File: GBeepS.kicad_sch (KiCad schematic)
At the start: 64 parts, among them J1 Ant, J2 BAT_TAB_POS, J3 BAT_TAB_NEGATIVE, Q1 PMZ130UNEYL, Q2 PMZ130UNEYL, Q3 DMN1025UFDB, Q4 PMZB320UPE, Q5 PMZB320UPE, U1 TCR3UG33A, U2 MMC3416xPJ, U3 ZOE-M8Q, U4 EFM8BB51F16G-A-QFN20, U5 BQ24040, U6 BQ29700, Y1 ECS-.327-7-16-TR3

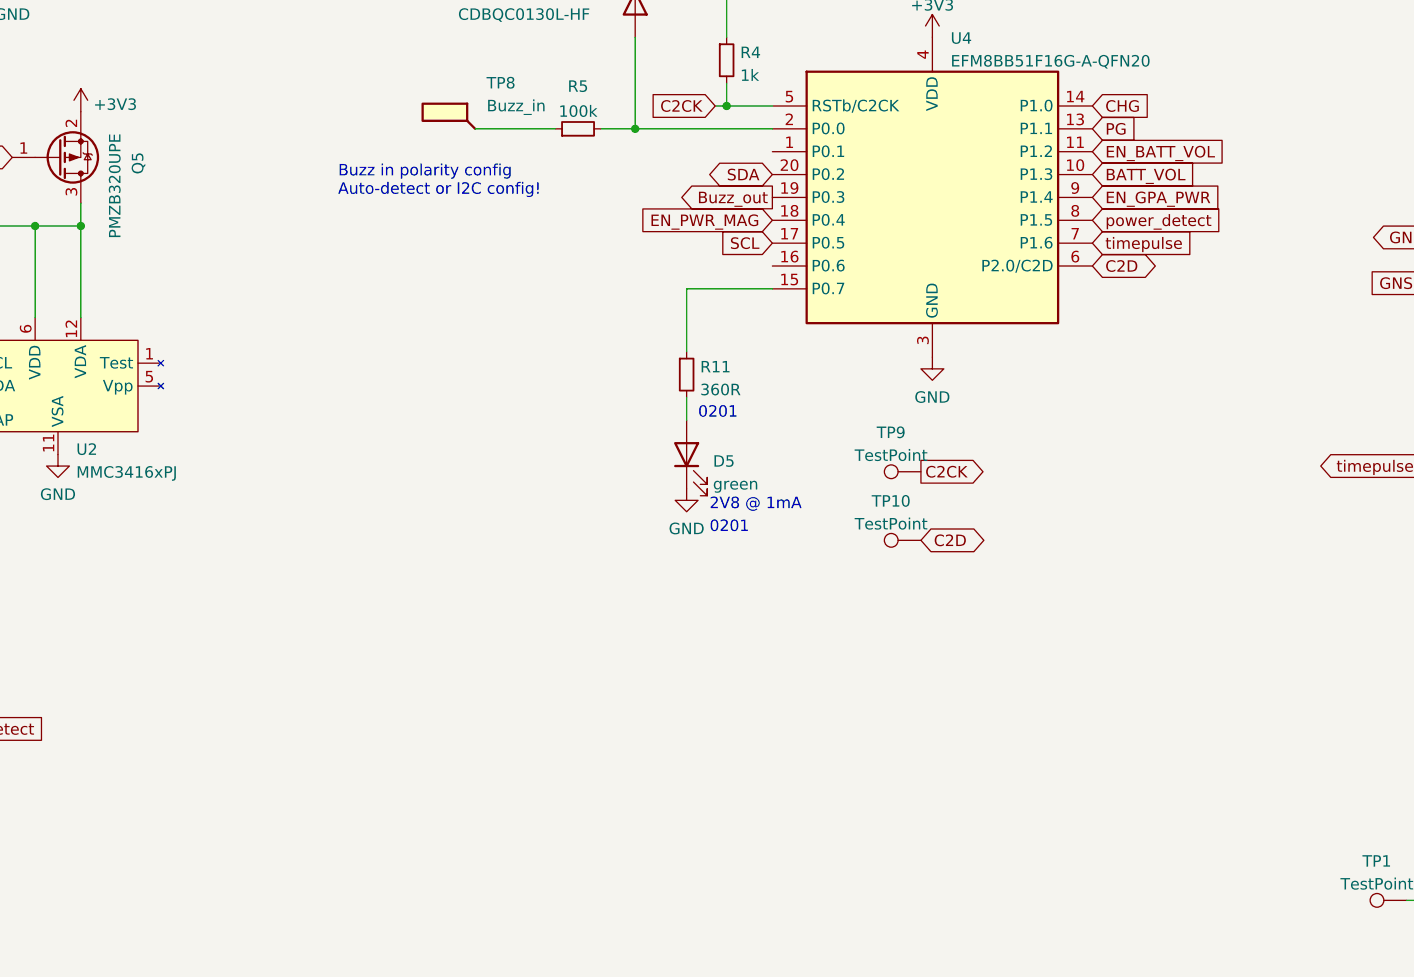
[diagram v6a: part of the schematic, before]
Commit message: added pushbutton and routed everything
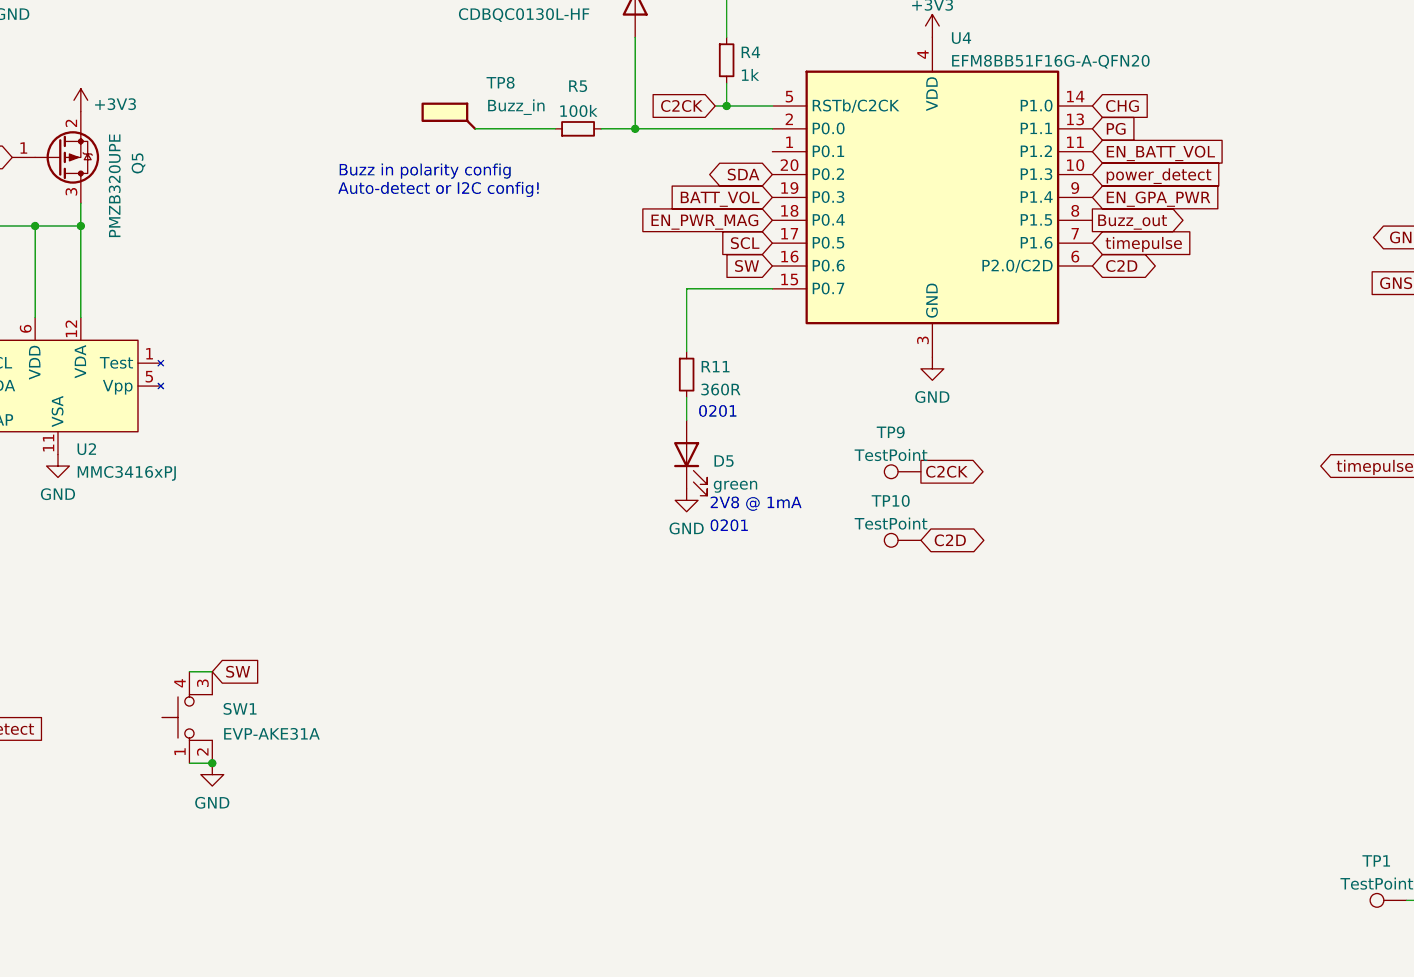
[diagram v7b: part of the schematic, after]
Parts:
- added SW1: EVP-AKE31A, Yolo-GPS:EVPAV, symbol Switch:SW_MEC_5E
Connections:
- net BATT_VOL: now also U4.19 (P0.3); no longer U4.10 (P1.3)
- net Buzz_out: now also U4.8 (P1.5); no longer U4.19 (P0.3)
- net GND: now also SW1.1, SW1.2
- net power_detect: now also U4.10 (P1.3); no longer U4.8 (P1.5)
- net SW: now reaches U4.16 (P0.6)
- net SW: now also SW1.3 (K), SW1.4 (A)
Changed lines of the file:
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@@
   (junction (at 179.705 262.255) (diameter 0) (color 0 0 0 0)
   )
+  (junction (at 95.885 130.81) (diameter 0) (color 0 0 0 0)
+  )
   (junction (at 179.705 243.205) (diameter 0) (color 0 0 0 0)
   )
@@
     (stroke (width 0) (type default) (color 0 0 0 0))
   )
+  (wire (pts (xy 93.345 130.81) (xy 95.885 130.81))
+    (stroke (width 0) (type default) (color 0 0 0 0))
+  )
   (wire (pts (xy 104.14 229.235) (xy 107.315 229.235))
     (stroke (width 0) (type default) (color 0 0 0 0))
@@
     (stroke (width 0) (type default) (color 0 0 0 0))
   )
+  (wire (pts (xy 93.345 120.65) (xy 95.885 120.65))
+    (stroke (width 0) (type default) (color 0 0 0 0))
+  )
   (wire (pts (xy 265.43 40.64) (xy 266.7 40.64))
     (stroke (width 0) (type default) (color 0 0 0 0))
@@
     )
   )
-  (global_label "Buzz_out" (shape output) (at 158.115 67.945 180) (fields_autoplaced)
-    (effects (font (size 1.27 1.27)) (justify right))
-    (property "Intersheet References" "${INTERSHEET_REFS}" (id 0) (at 147.2352 68.0244 0)
-      (effects (font (size 1.27 1.27)) (justify right) hide)
+  (global_label "Buzz_out" (shape output) (at 193.675 70.485 0) (fields_autoplaced)
+    (effects (font (size 1.27 1.27)) (justify left))
+    (property "Intersheet References" "${INTERSHEET_REFS}" (id 0) (at 204.5548 70.4056 0)
+      (effects (font (size 1.27 1.27)) (justify left) hide)
     )
   )
@@
     )
   )
+  (global_label "SW" (shape input) (at 158.115 75.565 180) (fields_autoplaced)
+    (effects (font (size 1.27 1.27)) (justify right))
+    (property "Intersheet References" "${INTERSHEET_REFS}" (id 0) (at 153.0409 75.6444 0)
+      (effects (font (size 1.27 1.27)) (justify right) hide)
+    )
+  )
   (global_label "EN_BATT_VOL" (shape input) (at 99.695 243.205 180) (fields_autoplaced)
     (effects (font (size 1.27 1.27)) (justify right))
@@
     )
   )
-  (global_label "BATT_VOL" (shape input) (at 193.675 65.405 0) (fields_autoplaced)
-    (effects (font (size 1.27 1.27)) (justify left))
-    (property "Intersheet References" "${INTERSHEET_REFS}" (id 0) (at 327.025 327.025 0)
+  (global_label "BATT_VOL" (shape input) (at 158.115 67.945 180) (fields_autoplaced)
+    (effects (font (size 1.27 1.27)) (justify right))
+    (property "Intersheet References" "${INTERSHEET_REFS}" (id 0) (at 24.765 -193.675 0)
       (effects (font (size 1.27 1.27)) hide)
     )
   )
+  (global_label "SW" (shape input) (at 95.885 120.65 0) (fields_autoplaced)
+    (effects (font (size 1.27 1.27)) (justify left))
+    (property "Intersheet References" "${INTERSHEET_REFS}" (id 0) (at 100.9591 120.5706 0)
+      (effects (font (size 1.27 1.27)) (justify left) hide)
+    )
+  )
   (global_label "SDA" (shape bidirectional) (at 158.115 65.405 180) (fields_autoplaced)
     (effects (font (size 1.27 1.27)) (justify right))
@@
     )
   )
-  (global_label "power_detect" (shape input) (at 193.675 70.485 0) (fields_autoplaced)
+  (global_label "power_detect" (shape input) (at 193.675 65.405 0) (fields_autoplaced)
     (effects (font (size 1.27 1.27)) (justify left))
-    (property "Intersheet References" "${INTERSHEET_REFS}" (id 0) (at 208.4252 70.4056 0)
+    (property "Intersheet References" "${INTERSHEET_REFS}" (id 0) (at 208.4252 65.3256 0)
       (effects (font (size 1.27 1.27)) (justify left) hide)
     )
@@
     (pin "1")
   )
+  (symbol (lib_id "power:GND") (at 95.885 130.81 0) (unit 1)
+    (in_bom yes) (on_board yes) (fields_autoplaced)
+    (property "Reference" "#PWR0123" (id 0) (at 95.885 137.16 0)
+      (effects (font (size 1.27 1.27)) hide)
+    )
+    (property "Value" "GND" (id 1) (at 95.885 135.2534 0))
+    (property "Footprint" "" (id 2) (at 95.885 130.81 0)
+      (effects (font (size 1.27 1.27)) hide)
+    )
+    (property "Datasheet" "" (id 3) (at 95.885 130.81 0)
+      (effects (font (size 1.27 1.27)) hide)
+    )
+    (pin "1")
+  )
+  (symbol (lib_id "Switch:SW_MEC_5E") (at 95.885 125.73 90) (unit 1)
+    (in_bom yes) (on_board yes) (fields_autoplaced)
+    (property "Reference" "SW1" (id 0) (at 97.028 124.8215 90)
+      (effects (font (size 1.27 1.27)) (justify right))
+    )
+    (property "Value" "EVP-AKE31A" (id 1) (at 97.028 127.5966 90)
+      (effects (font (size 1.27 1.27)) (justify right))
+    )
+    (property "Footprint" "Yolo-GPS:EVPAV" (id 2) (at 88.265 125.73 0)
+      (effects (font (size 1.27 1.27)) hide)
+    )
+    (property "Datasheet" "http://www.apem.com/int/index.php?controller=attachment&id_attachment=1371" (id 3) (at 88.265 125.73 0)
+      (effects (font (size 1.27 1.27)) hide)
+    )
+    (pin "1")
+    (pin "2")
+    (pin "3")
+    (pin "4")
+  )
   (symbol (lib_id "Device:Speaker") (at 63.5 218.44 0) (unit 1)
     (in_bom yes) (on_board yes) (fields_autoplaced)
@@
       (reference "#PWR0122") (unit 1) (value "GND") (footprint "")
     )
+    (path "/10f1abec-6492-4519-b5c7-3b2d41dddba6"
+      (reference "#PWR0123") (unit 1) (value "GND") (footprint "")
+    )
     (path "/15092cc1-4659-474f-baf6-7f47b7032fcf"
       (reference "#PWR0124") (unit 1) (value "GND") (footprint "")
@@
       (reference "R12") (unit 1) (value "300R") (footprint "Yolo-GPS:R_0201_0603Metric_mod")
     )
+    (path "/11677706-5f63-43f7-ad71-df2b977f82fd"
+      (reference "SW1") (unit 1) (value "EVP-AKE31A") (footprint "Yolo-GPS:EVPAV")
+    )
     (path "/c5da2475-a8cf-414e-aa2e-32063009c0e4"
